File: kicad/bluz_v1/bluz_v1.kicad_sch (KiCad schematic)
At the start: 61 parts, among them J1 USB_B_Micro, J10 Conn, J11 Conn, J12 BTAnt, J2 Conn, J3 Conn, J4 Conn, J5 Conn, J6 Conn, J7 Conn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

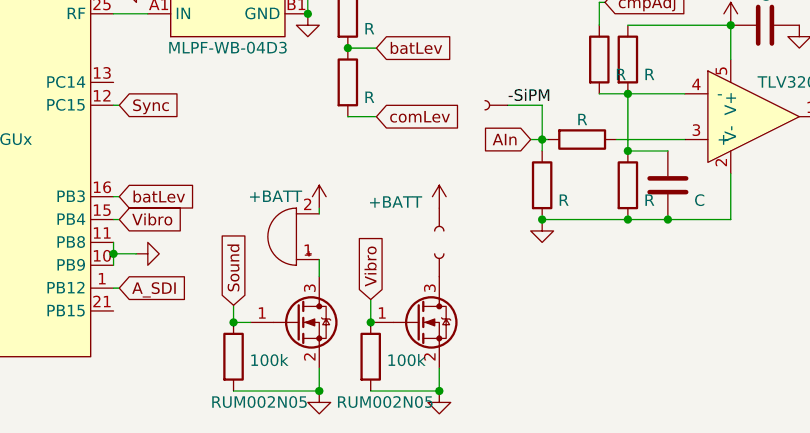
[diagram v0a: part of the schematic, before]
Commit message: удалено:       kicad/bluz_v1/bluz_v1-backups/bluz_v1-2024-05-03_143044.zip 	изменено:      kicad/bluz_v1/bluz_v1.kicad_pcb 	изменено:      kicad/bluz_v1/bluz_v1.kicad_prl 	изменено:      kicad/bluz_v1/bluz_v1.kicad_pro 	изменено:      kicad/bluz_v1/bluz_v1.kicad_sch
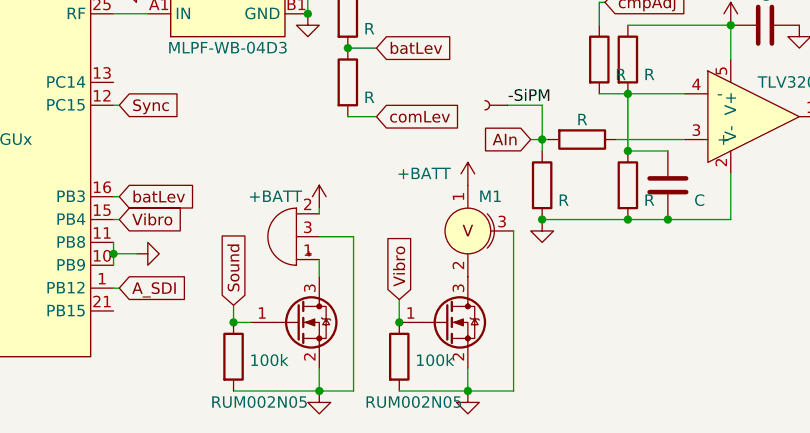
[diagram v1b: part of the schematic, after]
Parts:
- removed J10, J9: Conn, lib:conn_mini, symbol My-Library:Conn
- added M1: VibroMotor, MyLibrary:VibroMotor, symbol My_Library:VibroMotor
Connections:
- net +BATT: now also M1.1
- net GND: now also BZ1.3 (GND), M1.3
- net at Q2.3 (D): now also M1.2

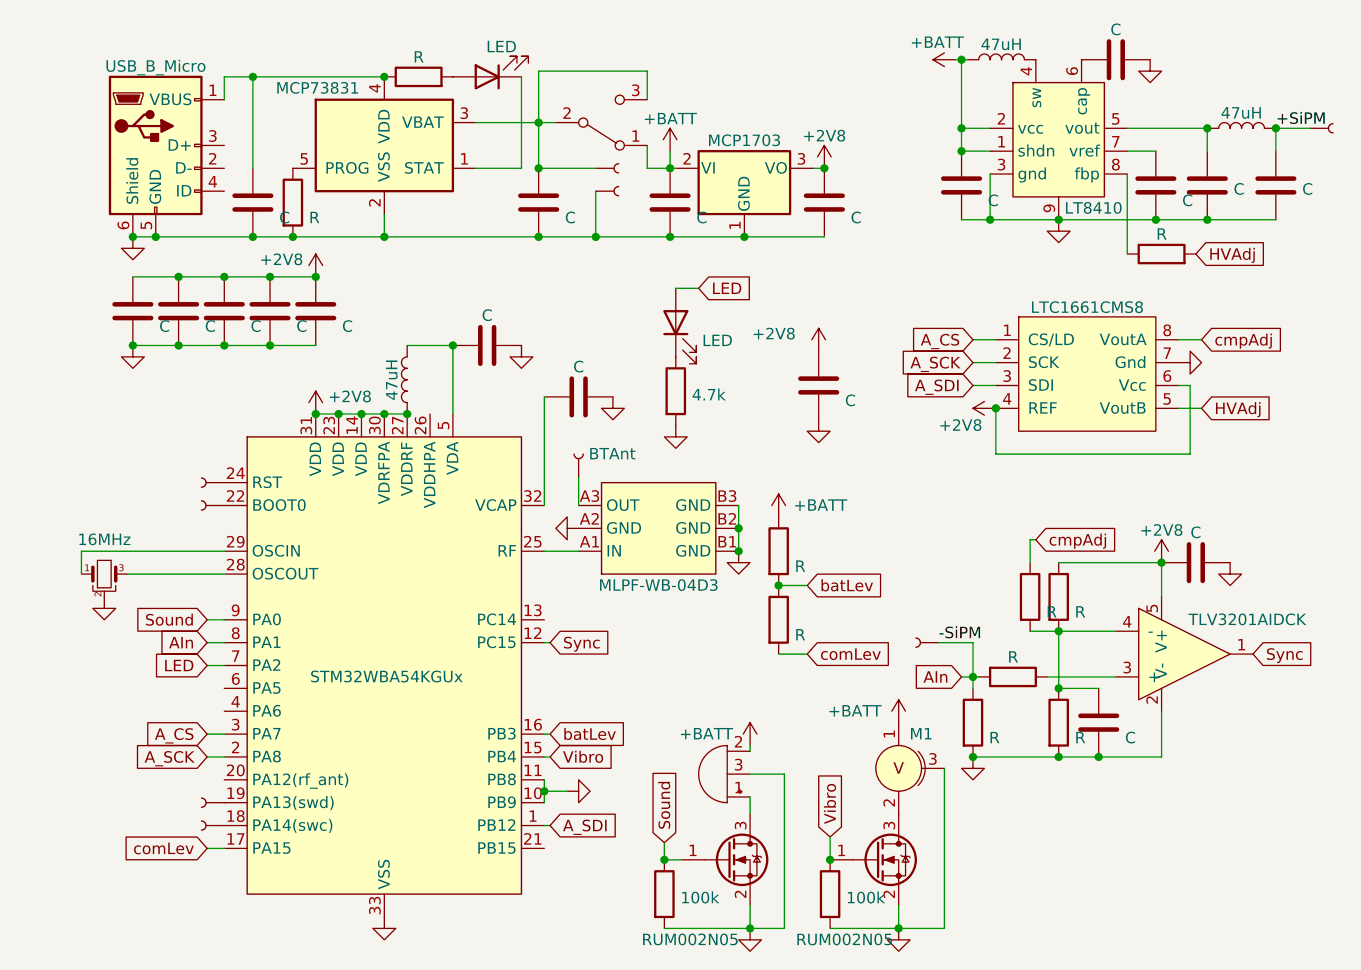
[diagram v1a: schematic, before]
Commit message: новый файл:    Documents/NX2016AB-32MHZ ST2.pdf 	новый файл:    Documents/NX2016SA-2_e.pdf 	новый файл:    Documents/stm32wba-nucleo64-mb1863.pdf 	изменено:      kicad/bluz_v1/bluz_v1.kicad_pcb 	изменено:      kicad/bluz_v1/bluz_v1.kicad_sch
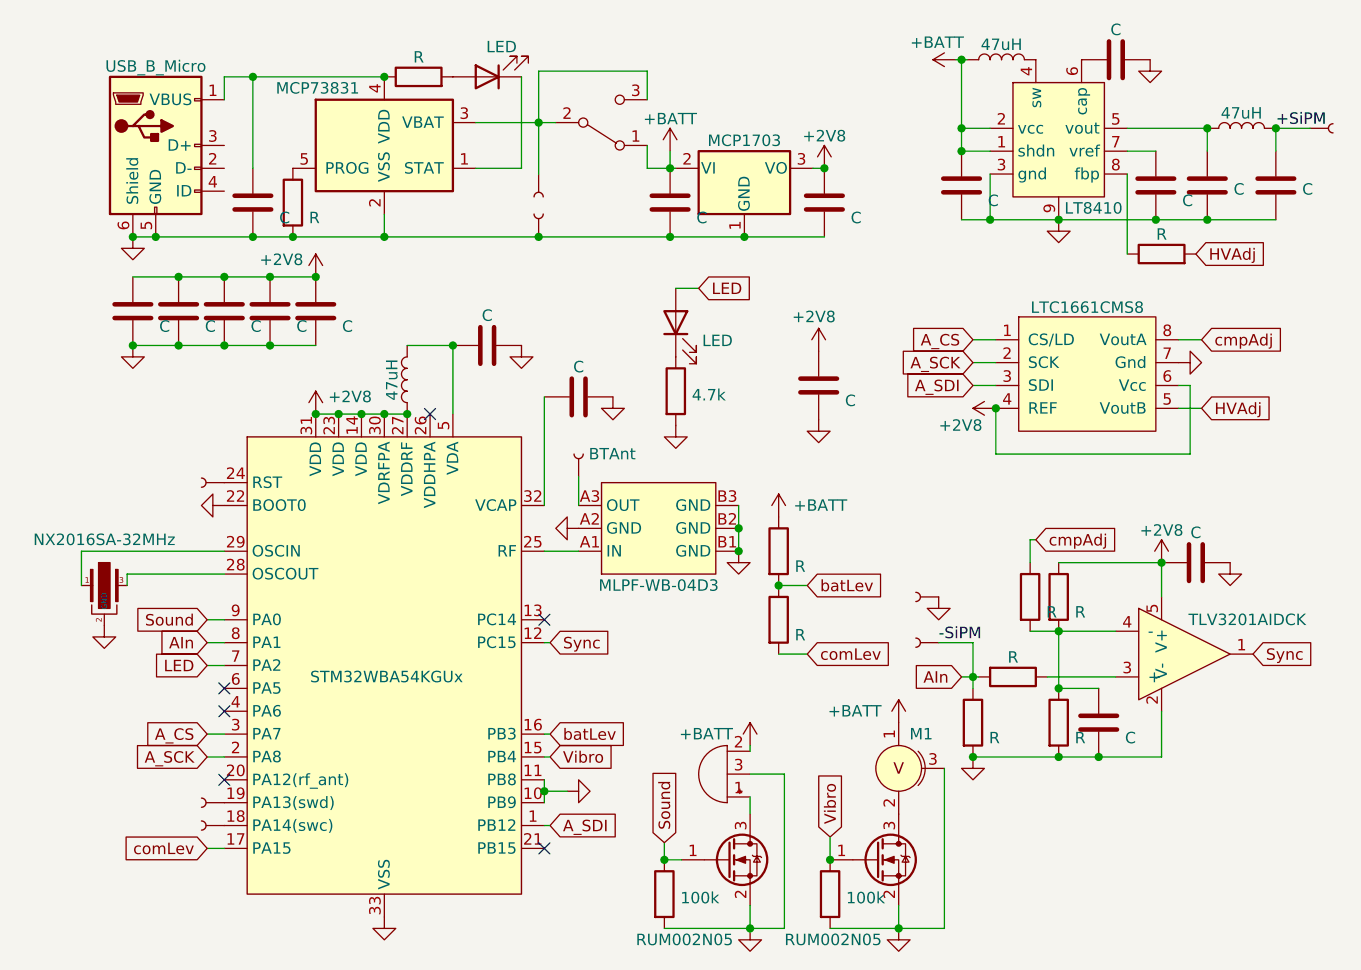
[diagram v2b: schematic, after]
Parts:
- removed C9: C, Capacitor_SMD:C_0402_1005Metric, symbol Device:C
- removed Y1: 16MHz, Crystal:Resonator_SMD_Murata_CSTxExxV-3Pin_3.0x1.1mm, symbol Device:Crystal_GND2_Small
- added Y1: NX2016SA-32MHz, Crystal:Crystal_SMD_2016-4Pin_2.0x1.6mm, symbol My-Library:NX2016SA
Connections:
- net GND: now also D1.22 (BOOT0), J3.1, Y1.2 (GND), Y1.4 (GND)
- net at D1.28 (OSCOUT): now also Y1.3
- net at D1.29 (OSCIN): now also Y1.1
- no-connect marks 0 -> 6

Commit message: удалено:       kicad/bluz_v1/bluz_v1-backups/bluz_v1-2024-04-18_173246.zip 	удалено:       kicad/bluz_v1/bluz_v1-backups/bluz_v1-2024-04-18_175303.zip 	удалено:       kicad/bluz_v1/bluz_v1-backups/bluz_v1-2024-04-18_180313.zip 	изменено:      kicad/bluz_v1/bluz_v1.kicad_pcb 	изменено:      kicad/bluz_v1/bluz_v1.kicad_sch 	изменено:      kicad/bluz_v1/fp-info-cache
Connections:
- net at C4.1, J1.1 (VBUS), U1.4 (VDD): now also D2.2 (A); no longer R4.1
- net at R4.2: now also U1.1 (STAT); no longer D2.2 (A)
- net at D2.1 (K): now also R4.1; no longer U1.1 (STAT)
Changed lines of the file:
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@@
   (junction (at 194.945 34.925) (diameter 0) (color 0 0 0 0)
   )
+  (junction (at 103.505 29.21) (diameter 0) (color 0 0 0 0)
+  )
   (junction (at 111.125 59.055) (diameter 0) (color 0 0 0 0)
   )
@@
   )
   (junction (at 178.435 45.085) (diameter 0) (color 0 0 0 0)
-  )
-  (junction (at 103.505 29.21) (diameter 0) (color 0 0 0 0)
   )
   (junction (at 85.725 51.435) (diameter 0) (color 0 0 0 0)
@@
     (pin "2")
   )
-  (symbol (lib_id "Device:R") (at 107.315 29.21 90) (unit 1)
-    (in_bom yes) (on_board yes) (fields_autoplaced)
-    (property "Reference" "R4" (id 0) (at 107.315 24.4942 90)
-      (effects (font (size 1.27 1.27)) hide)
-    )
-    (property "Value" "R" (id 1) (at 107.315 27.0311 90))
-    (property "Footprint" "Resistor_SMD:R_0402_1005Metric" (id 2) (at 107.315 30.988 90)
-      (effects (font (size 1.27 1.27)) hide)
-    )
-    (property "Datasheet" "~" (id 3) (at 107.315 29.21 0)
+  (symbol (lib_id "Device:R") (at 114.935 29.21 90) (unit 1)
+    (in_bom yes) (on_board yes) (fields_autoplaced)
+    (property "Reference" "R4" (id 0) (at 114.935 24.4942 90)
+      (effects (font (size 1.27 1.27)) hide)
+    )
+    (property "Value" "R" (id 1) (at 114.935 27.0311 90))
+    (property "Footprint" "Resistor_SMD:R_0402_1005Metric" (id 2) (at 114.935 30.988 90)
+      (effects (font (size 1.27 1.27)) hide)
+    )
+    (property "Datasheet" "~" (id 3) (at 114.935 29.21 0)
       (effects (font (size 1.27 1.27)) hide)
     )
@@
     (pin "2")
   )
-  (symbol (lib_id "Device:LED") (at 114.935 29.21 180) (unit 1)
-    (in_bom yes) (on_board yes) (fields_autoplaced)
-    (property "Reference" "D2" (id 0) (at 116.5225 23.3512 0)
-      (effects (font (size 1.27 1.27)) hide)
-    )
-    (property "Value" "LED" (id 1) (at 116.5225 25.8882 0))
-    (property "Footprint" "LED_SMD:LED_0402_1005Metric" (id 2) (at 114.935 29.21 0)
-      (effects (font (size 1.27 1.27)) hide)
-    )
-    (property "Datasheet" "~" (id 3) (at 114.935 29.21 0)
-      (effects (font (size 1.27 1.27)) hide)
-    )
+  (symbol (lib_id "Device:LED") (at 107.315 29.21 180) (unit 1)
+    (in_bom yes) (on_board yes) (fields_autoplaced)
+    (property "Reference" "D2" (id 0) (at 108.9025 23.3512 0)
+      (effects (font (size 1.27 1.27)) hide)
+    )
+    (property "Value" "LED" (id 1) (at 108.9025 25.8882 0))
+    (property "Footprint" "LED_SMD:LED_0402_1005Metric" (id 2) (at 107.315 29.21 0)
+      (effects (font (size 1.27 1.27)) hide)
+    )
+    (property "Datasheet" "~" (id 3) (at 107.315 29.21 0)
+      (effects (font (size 1.27 1.27)) hide)
+    )

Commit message: изменено:      kicad/bluz_v1/bluz_v1.kicad_pcb 	изменено:      kicad/bluz_v1/bluz_v1.kicad_prl 	изменено:      kicad/bluz_v1/bluz_v1.kicad_sch
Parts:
- removed U2: MCP1703, Package_TO_SOT_SMD:SOT-23W, symbol Regulator_Linear:MCP1703Ax-180xxMB
- added U2: MCP1700, Package_TO_SOT_SMD:SOT-23, symbol Regulator_Linear:MCP1700x-280xxTT
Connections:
- net +2V8: now also U2.2 (VO)
- net +BATT: now also U2.3 (VI)
- net GND: now also U2.1 (GND)

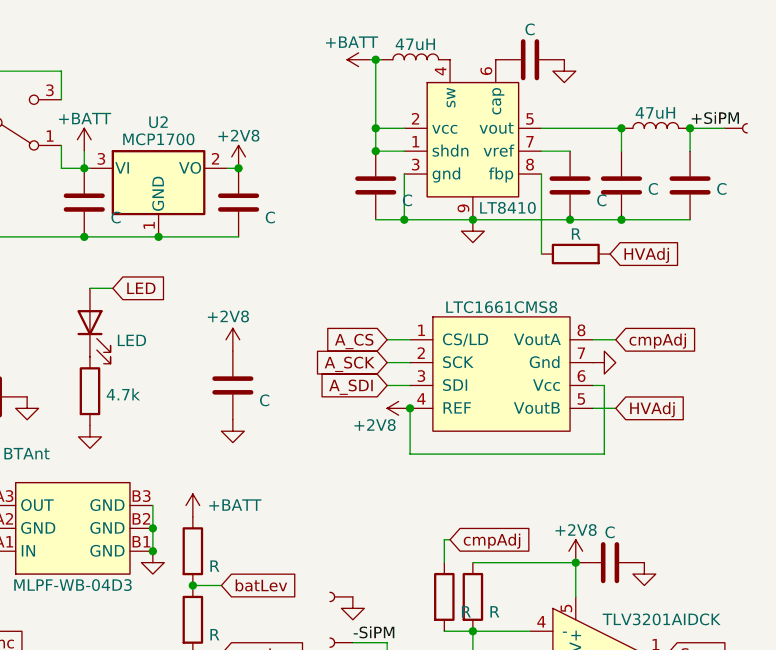
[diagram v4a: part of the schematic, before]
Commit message: удалено:       kicad/bluz_v1/bluz_v1-backups/bluz_v1-2024-04-18_190147.zip 	удалено:       kicad/bluz_v1/bluz_v1-backups/bluz_v1-2024-04-19_183106.zip 	удалено:       kicad/bluz_v1/bluz_v1-backups/bluz_v1-2024-04-19_183722.zip 	удалено:       kicad/bluz_v1/bluz_v1-backups/bluz_v1-2024-04-19_184242.zip 	удалено:       kicad/bluz_v1/bluz_v1-backups/bluz_v1-2024-04-19_185221.zip 	изменено:      kicad/bluz_v1/bluz_v1.kicad_pcb 	изменено:      kicad/bluz_v1/bluz_v1.kicad_prl 	изменено:      kicad/bluz_v1/bluz_v1.kicad_sch 	изменено:      kicad/bluz_v1/fp-info-cache 	Documents/rm0493-multiprotocol-wireless-bluetooth-lowenergy-and-ieee802154-stm32wba5xxx-armbased-32bit-mcus-stmicroelectronics.pdf 	Documents/tn1163-description-of-wlcsp-for-microcontrollers-and-recommendations-for-its-use-stmicroelectronics.pdf
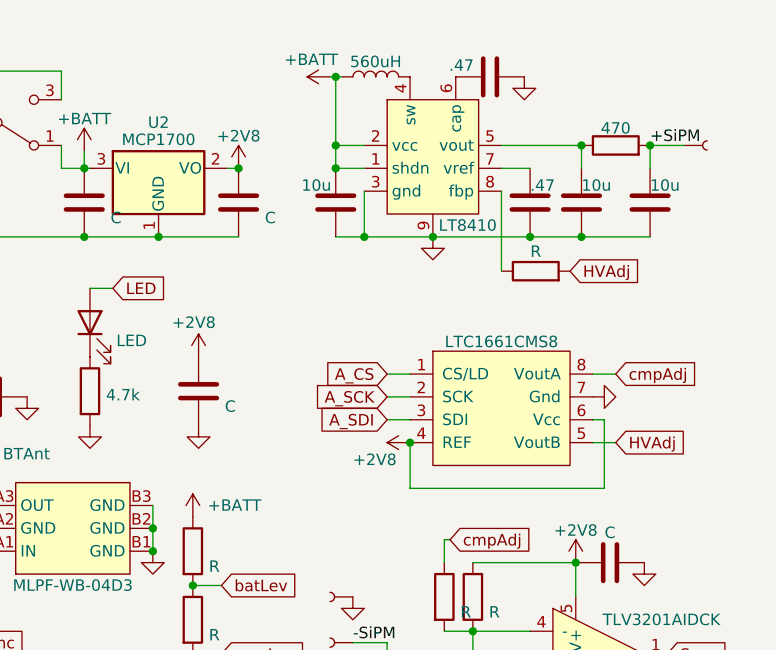
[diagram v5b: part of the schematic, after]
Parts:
- removed L3: 47uH, Inductor_SMD:L_0603_1608Metric, symbol Device:L
- added R14: 470, Resistor_SMD:R_0402_1005Metric, symbol Device:R
- C15: value C -> 10u
- C16, C17: value C -> .47
- C18, C19: value C -> 10u; footprint Capacitor_SMD:C_0805_2012Metric -> Capacitor_SMD:C_1206_3216Metric
- L2: value 47uH -> 560uH; footprint Inductor_SMD:L_1210_3225Metric -> Inductor_SMD:L_1206_3216Metric
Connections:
- net +SiPM: now also R14.2
- net at C18.2, D5.5 (vout): now also R14.1

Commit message: удалено:       kicad/bluz_v1/bluz_v1-backups/bluz_v1-2024-04-19_190122.zip 	удалено:       kicad/bluz_v1/bluz_v1-backups/bluz_v1-2024-04-22_153028.zip 	удалено:       kicad/bluz_v1/bluz_v1-backups/bluz_v1-2024-04-26_142701.zip 	удалено:       kicad/bluz_v1/bluz_v1-backups/bluz_v1-2024-05-03_144119.zip 	удалено:       kicad/bluz_v1/bluz_v1-backups/bluz_v1-2024-05-03_145331.zip 	изменено:      kicad/bluz_v1/bluz_v1.kicad_pcb 	изменено:      kicad/bluz_v1/bluz_v1.kicad_sch 	изменено:      kicad/bluz_v1/fp-info-cache
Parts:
- removed C17: .47, Capacitor_SMD:C_0402_1005Metric, symbol Device:C
- removed C18: 10u, Capacitor_SMD:C_1206_3216Metric, symbol Device:C
- removed D5: LT8410, Package_DFN_QFN:DFN-8-1EP_2x2mm_P0.45mm_EP0.64x1.38mm, symbol My-Library:LT8410
- added C9: 1.5p, Capacitor_SMD:C_0402_1005Metric, symbol Device:C
- added D5: BAT46JFILM, Diode_SMD:D_SOD-323, symbol Device:D
- added R15: 4.3M, Resistor_SMD:R_0402_1005Metric, symbol Device:R
- added R16: 100M, Resistor_SMD:R_0603_1608Metric, symbol Device:R
- added U4: AP3015KTR, Package_TO_SOT_SMD:SOT-23-5, symbol My_Library:AP3015KTR
- BZ1: footprint lib:Buzzer5x5 -> MyLibrary:Buzzer55x55
- C16: value .47 -> 10u; footprint Capacitor_SMD:C_0402_1005Metric -> Capacitor_SMD:C_0805_2012Metric
- C19: footprint Capacitor_SMD:C_1206_3216Metric -> Capacitor_SMD:C_0805_2012Metric
- L2: value 560uH -> 220uH
- R13: value R -> 100M
- U2: footprint Package_TO_SOT_SMD:SOT-23 -> Package_TO_SOT_SMD:SOT-23-3
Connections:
- net +BATT: now also U4.4 (EN), U4.5 (VIN)
- net GND: now also C16.1, R15.2, U4.2 (GND); no longer C16.2
- net at L2.2: now also D5.2 (A), U4.1 (SW)
- net at R14.1: now also C16.2, C9.1, D5.1 (K), R16.1
- net at R13.1: now also C9.2, R15.1, R16.2, U4.3 (FB)

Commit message: изменено:      Documents/BluZ.png 	удалено:       kicad/bluz_v1/bluz_v1-backups/bluz_v1-2024-05-03_150608.zip 	удалено:       kicad/bluz_v1/bluz_v1-backups/bluz_v1-2024-05-03_151512.zip 	удалено:       kicad/bluz_v1/bluz_v1-backups/bluz_v1-2024-05-03_172047.zip 	изменено:      kicad/bluz_v1/bluz_v1.kicad_pcb 	изменено:      kicad/bluz_v1/bluz_v1.kicad_sch 	изменено:      kicad/bluz_v1/fp-info-cache
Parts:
- added C17: C, Capacitor_SMD:C_0402_1005Metric, symbol Device:C
- R16: footprint Resistor_SMD:R_0603_1608Metric -> Resistor_SMD:R_0402_1005Metric
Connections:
- net +BATT: now also BZ1.1 (-); no longer BZ1.2 (+)
- net GND: now also C17.2
- net at Q1.3 (D): now also BZ1.2 (+); no longer BZ1.1 (-)
- net at D1.26 (VDDHPA): now also C17.1
- net B+: now reaches J6.1, SW1.2 (B), SW1.3 (C), U1.3 (VBAT)
- no-connect marks 6 -> 5
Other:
- moved on the sheet: U2
